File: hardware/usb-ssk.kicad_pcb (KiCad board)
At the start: 4 copper layers, 30 x 30 mm, 44 parts, among them J101 XZ, J102 YZ, J103 IN, J201 USB_C_Receptacle_USB2.0, J301 TAGCONNECT, SW301 DFU, U201 SRV05-4, U301 STM32G431, U401 XC6206P182MR_C347373, U501 IIS2ICLXTR

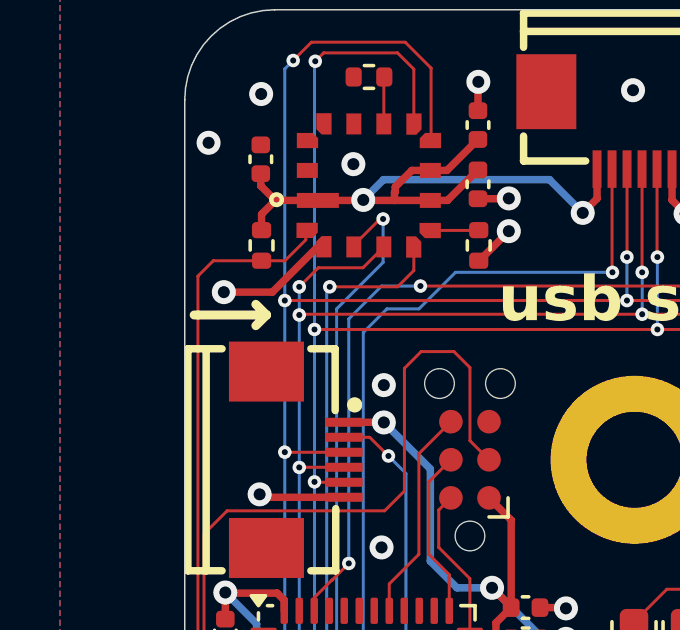
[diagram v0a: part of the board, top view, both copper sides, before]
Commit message: add dimensions to pcb
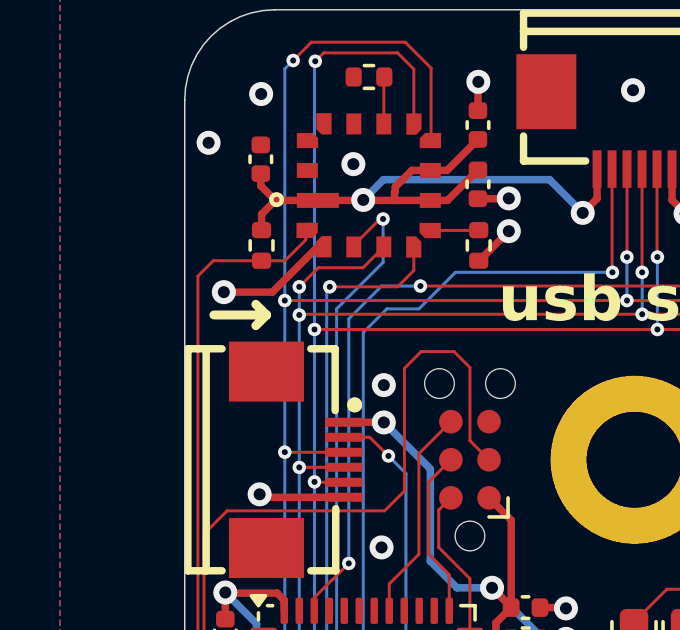
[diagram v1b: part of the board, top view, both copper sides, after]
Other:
- board text added: "mateijordache"
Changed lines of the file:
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@@
 	)
 	(paper "A4")
+	(title_block
+		(title "USB SSK")
+		(date "2024-10-30")
+		(rev "1.0")
+		(company "asylum research")
+		(comment 1 "matei jordache")
+	)
 	(layers
 		(0 "F.Cu" signal)
@@
 	)
 	(gr_line
-		(start 133.1976 105.0036)
+		(start 133.858 105.0036)
 		(end 135.6106 105.0036)
 		(stroke
@@
 		)
 	)
+	(gr_text "mateijordache"
+		(at 161.3408 97.3328 0)
+		(layer "B.Mask")
+		(effects
+			(font
+				(size 1 1)
+				(thickness 0.25)
+				(bold yes)
+			)
+			(justify left bottom mirror)
+		)
+	)
 	(gr_text "x"
 		(at 154.5336 112.268 0)
@@
 		)
 	)
+	(dimension
+		(type aligned)
+		(layer "Dwgs.User")
+		(pts
+			(xy 147.8788 109.8296) (xy 147.8788 94.8296)
+		)
+		(height 25.146)
+		(gr_text "15.0 mm"
+			(at 171.8748 102.3296 90)
+			(layer "Dwgs.User")
+			(effects
+				(font
+					(size 1 1)
+					(thickness 0.15)
+				)
+			)
+		)
+		(format
+			(prefix "")
+			(suffix "")
+			(units 3)
+			(units_format 1)
+			(precision 1)
+		)
+		(style
+			(thickness 0.15)
+			(arrow_length 1.27)
+			(text_position_mode 0)
+			(extension_height 0.58642)
+			(extension_offset 0.5) keep_text_aligned)
+	)
+	(dimension
+		(type aligned)
+		(layer "Dwgs.User")
+		(pts
+			(xy 147.8788 109.8296) (xy 162.885598 109.8296)
+		)
+		(height -22.3012)
+		(gr_text "15.0 mm"
+			(at 155.382199 86.3784 0)
+			(layer "Dwgs.User")
+			(effects
+				(font
+					(size 1 1)
+					(thickness 0.15)
+				)
+			)
+		)
+		(format
+			(prefix "")
+			(suffix "")
+			(units 3)
+			(units_format 1)
+			(precision 1)
+		)
+		(style
+			(thickness 0.15)
+			(arrow_length 1.27)
+			(text_position_mode 0)
+			(extension_height 0.58642)
+			(extension_offset 0.5) keep_text_aligned)
+	)
+	(dimension
+		(type aligned)
+		(layer "Dwgs.User")
+		(pts
+			(xy 159.885598 94.8296) (xy 159.885598 124.8296)
+		)
+		(height -18.371602)
+		(gr_text "30.0 mm"
+			(at 177.1072 109.8296 90)
+			(layer "Dwgs.User")
+			(effects
+				(font
+					(size 1 1)
+					(thickness 0.15)
+				)
+			)
+		)
+		(format
+			(prefix "")
+			(suffix "")
+			(units 3)
+			(units_format 1)
+			(precision 1)
+		)
+		(style
+			(thickness 0.15)
+			(arrow_length 1.27)
+			(text_position_mode 0)
+			(extension_height 0.58642)
+			(extension_offset 0.5) keep_text_aligned)
+	)
+	(dimension
+		(type aligned)
+		(layer "Dwgs.User")
+		(pts
+			(xy 132.885598 97.8296) (xy 162.885598 97.8296)
+		)
+		(height -13.7048)
+		(gr_text "30.0 mm"
+			(at 147.885598 82.9748 0)
+			(layer "Dwgs.User")
+			(effects
+				(font
+					(size 1 1)
+					(thickness 0.15)
+				)
+			)
+		)
+		(format
+			(prefix "")
+			(suffix "")
+			(units 3)
+			(units_format 1)
+			(precision 1)
+		)
+		(style
+			(thickness 0.15)
+			(arrow_length 1.27)
+			(text_position_mode 0)
+			(extension_height 0.58642)
+			(extension_offset 0.5) keep_text_aligned)
+	)
+	(dimension
+		(type leader)
+		(layer "Dwgs.User")
+		(pts
+			(xy 133.764278 123.95092) (xy 127 130.715198)
+		)
+		(gr_text "4x R 3 mm"
+			(at 114.3 130.715198 0)
+			(layer "Dwgs.User")
+			(effects
+				(font
+					(size 1 1)
+					(thickness 0.15)
+				)
+			)
+		)
+		(format
+			(prefix "")
+			(suffix "")
+			(units 0)
+			(units_format 0)
+			(precision 4)
+			(override_value "4x R 3 mm")
+		)
+		(style
+			(thickness 0.15)
+			(arrow_length 1.27)
+			(text_position_mode 0)
+			(text_frame 0)
+			(extension_offset 0.5)
+		)
+	)
